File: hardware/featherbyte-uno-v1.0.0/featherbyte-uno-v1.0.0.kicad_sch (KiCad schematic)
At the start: 60 parts, among them J1 Conn_01x08, J10 Conn_01x09, J2 Conn_01x10, J3 Conn_01x06, J5 USB_C_Receptacle_16P, J6 SWD Connector, J7 Terminal Block, J8 USB_C_Receptacle_16P, J9 BOOT1, SW1 Reset, SW2 BOOT0, SW3 SW_DIP_x04, U1 CH32V203CxT6, U2 TJA1050, U4 AMS1117-3.3, U5 USBLC6-2P6, U6 USBLC6-2P6, Y1 8M, Y3 32.768K

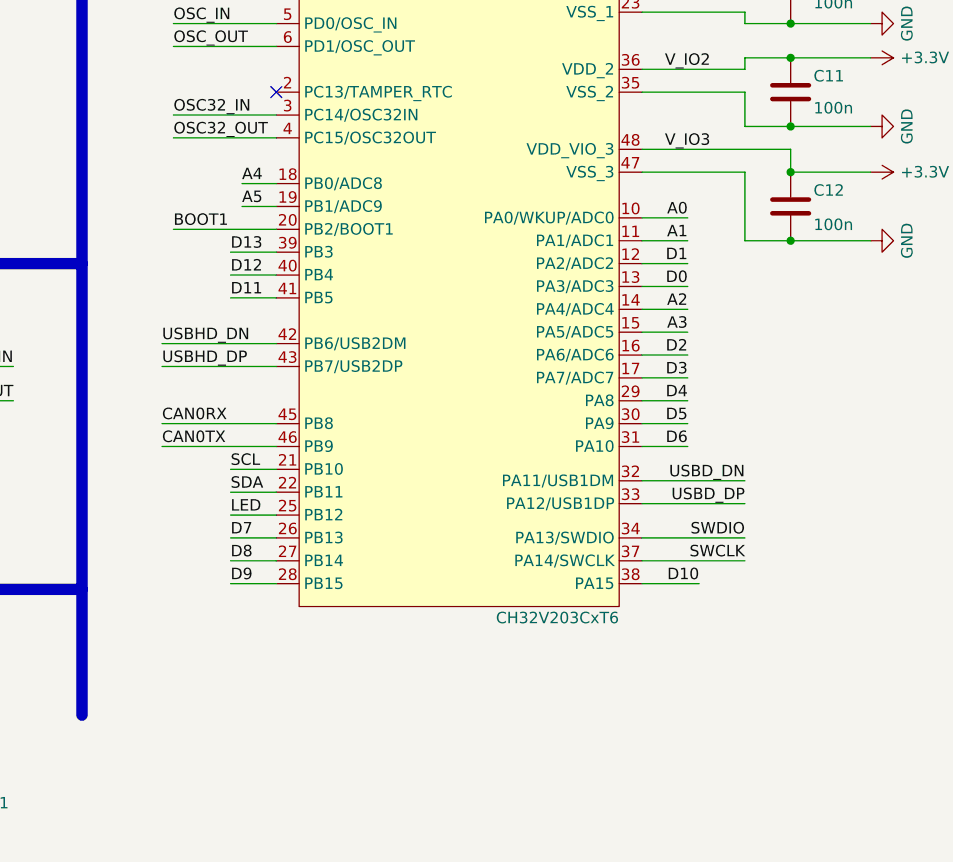
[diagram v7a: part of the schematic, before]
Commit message: pin arrangement changes required
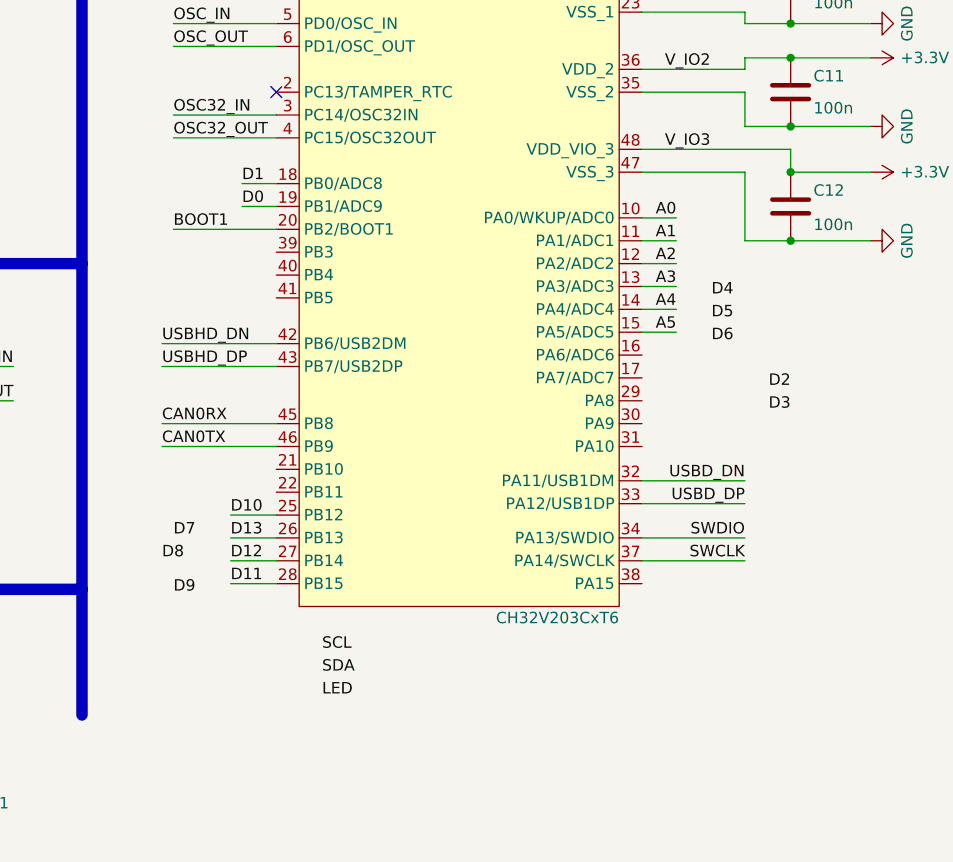
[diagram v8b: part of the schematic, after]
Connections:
- net A2: now also U1.12 (PA2/ADC2); no longer U1.14 (PA4/ADC4)
- net A3: now also U1.13 (PA3/ADC3); no longer U1.15 (PA5/ADC5)
- net A4: now also U1.14 (PA4/ADC4); no longer U1.18 (PB0/ADC8)
- net A5: now also U1.15 (PA5/ADC5); no longer U1.19 (PB1/ADC9)
- net D0: now also U1.19 (PB1/ADC9); no longer U1.13 (PA3/ADC3)
- net D1: now also U1.18 (PB0/ADC8); no longer U1.12 (PA2/ADC2)
- net D10: now also U1.25 (PB12); no longer U1.38 (PA15)
- net D11: now also U1.28 (PB15); no longer U1.41 (PB5)
- net D12: now also U1.27 (PB14); no longer U1.40 (PB4)
- net D13: now also U1.26 (PB13); no longer U1.39 (PB3)
- net D2: no longer U1.16 (PA6/ADC6)
- net D3: no longer U1.17 (PA7/ADC7)
- net D4: no longer U1.29 (PA8)
- net D5: no longer U1.30 (PA9)
- net D6: no longer U1.31 (PA10)
- net D7: no longer U1.26 (PB13)
- net D8: no longer U1.27 (PB14)
- net D9: no longer U1.28 (PB15)
- net LED: no longer U1.25 (PB12)
- net SCL: no longer U1.21 (PB10)
- net SDA: no longer U1.22 (PB11)
